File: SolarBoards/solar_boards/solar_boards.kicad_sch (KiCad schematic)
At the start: 37 parts, among them J1 M55-6001242R, U1 LTC3105EDD-TRPBF, U2 OPT3004DNPR, U3 LM73100RPWR

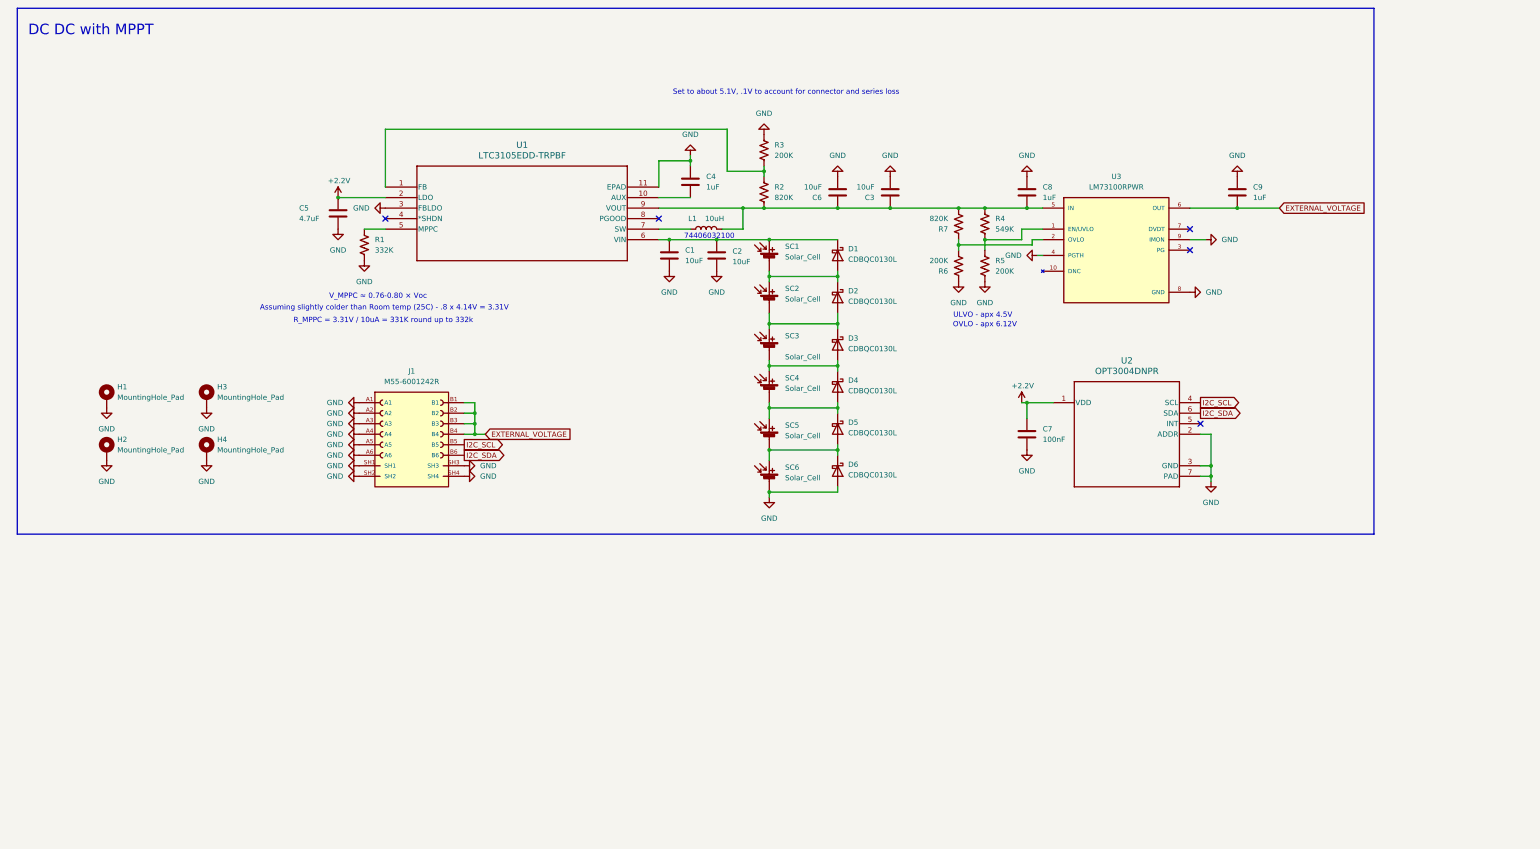
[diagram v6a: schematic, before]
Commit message: Routing and schematic work on most boards
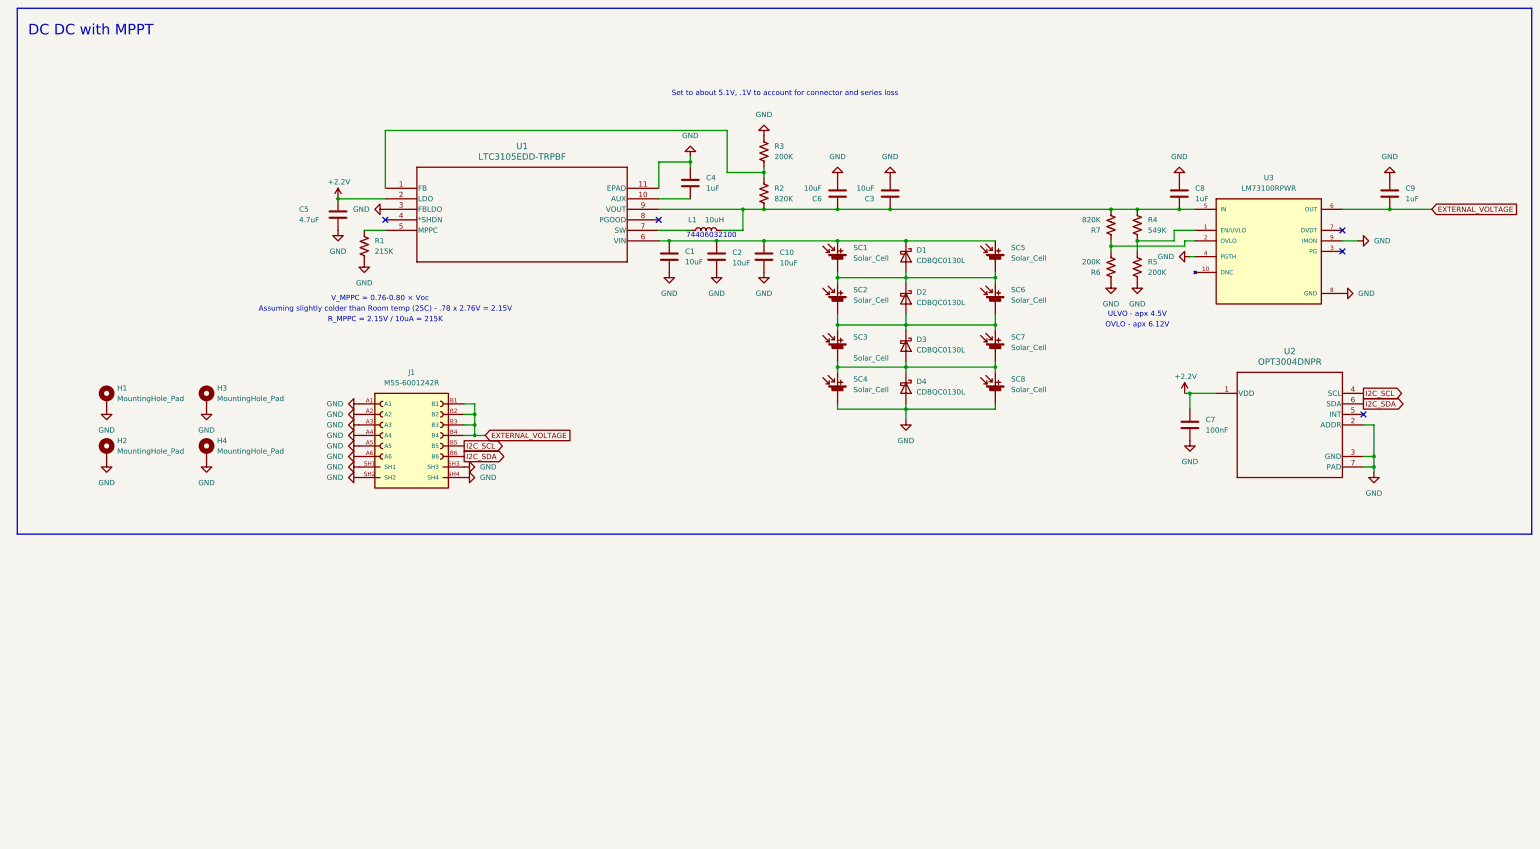
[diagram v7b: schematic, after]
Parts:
- removed D5, D6: CDBQC0130L, inspireFly:DIODFN100X60X55-2N, symbol Device:D_Schottky
- added C10: 10uF, Capacitor_SMD:C_0603_1608Metric, symbol Device:C
- added SC7, SC8: Solar_Cell, inspireFly:SOLAR_KXOB25-14X1F-TR, symbol Device:Solar_Cell
- C1, C2, C3, C6: footprint Capacitor_SMD:C_0402_1005Metric_Pad0.74x0.62mm_HandSolder -> Capacitor_SMD:C_0603_1608Metric
- R1: value 332K -> 215K
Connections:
- net GND: now also D4.2 (A), SC4.2 (-), C10.2, SC8.2 (-); no longer SC6.2 (-)
- net at C1.1, C2.1, D1.1 (K)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: now also SC5.1 (+), C10.1
- net at D1.2 (A), D2.1 (K), SC1.2 (-)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: now also SC5.2 (-), SC6.1 (+)
- net at D2.2 (A), D3.1 (K), SC2.2 (-)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: now also SC6.2 (-), SC7.1 (+)
- net at D3.2 (A), D4.1 (K), SC3.2 (-)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: now also SC7.2 (-), SC8.1 (+)
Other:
- note added: "Assuming slightly colder than Room temp (25C) - .78 x 2.76V = 2.15V"
- note added: "R_MPPC = 2.15V / 10uA = 215K"
- note removed: "Assuming slightly colder than Room temp (25C) - .8 x 4.14V = 3.31V"
- note removed: "R_MPPC = 3.31V / 10uA = 331K round up to 332k"
- moved on the sheet: C7, C8, C9, D1, D2, D3, D4, R4, R5, R6, R7, SC1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

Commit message: Finalize board work + BOM work
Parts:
- C5: footprint Capacitor_SMD:C_0402_1005Metric_Pad0.74x0.62mm_HandSolder -> Capacitor_SMD:C_0603_1608Metric
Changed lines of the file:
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@@
 			)
 		)
-		(property "Footprint" "Capacitor_SMD:C_0402_1005Metric_Pad0.74x0.62mm_HandSolder"
+		(property "Footprint" "Capacitor_SMD:C_0603_1608Metric"
 			(at 89.8652 66.04 0)
 			(hide yes)
